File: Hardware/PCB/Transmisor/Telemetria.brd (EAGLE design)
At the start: 74.9 x 87.3 mm, 15 parts, among them X3 JST-XH-05-PIN-LONG-PAD

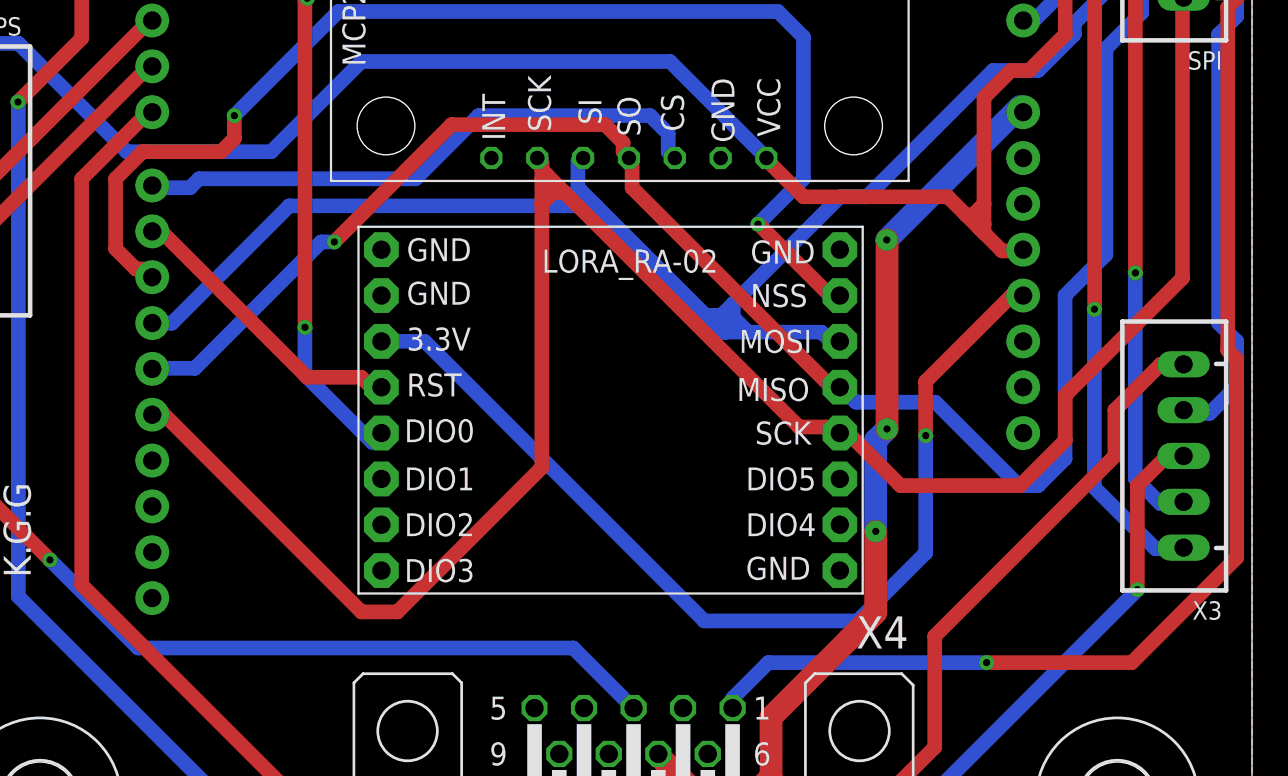
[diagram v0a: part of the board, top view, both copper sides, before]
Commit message: fix(transmissor): transmisson pcb updated
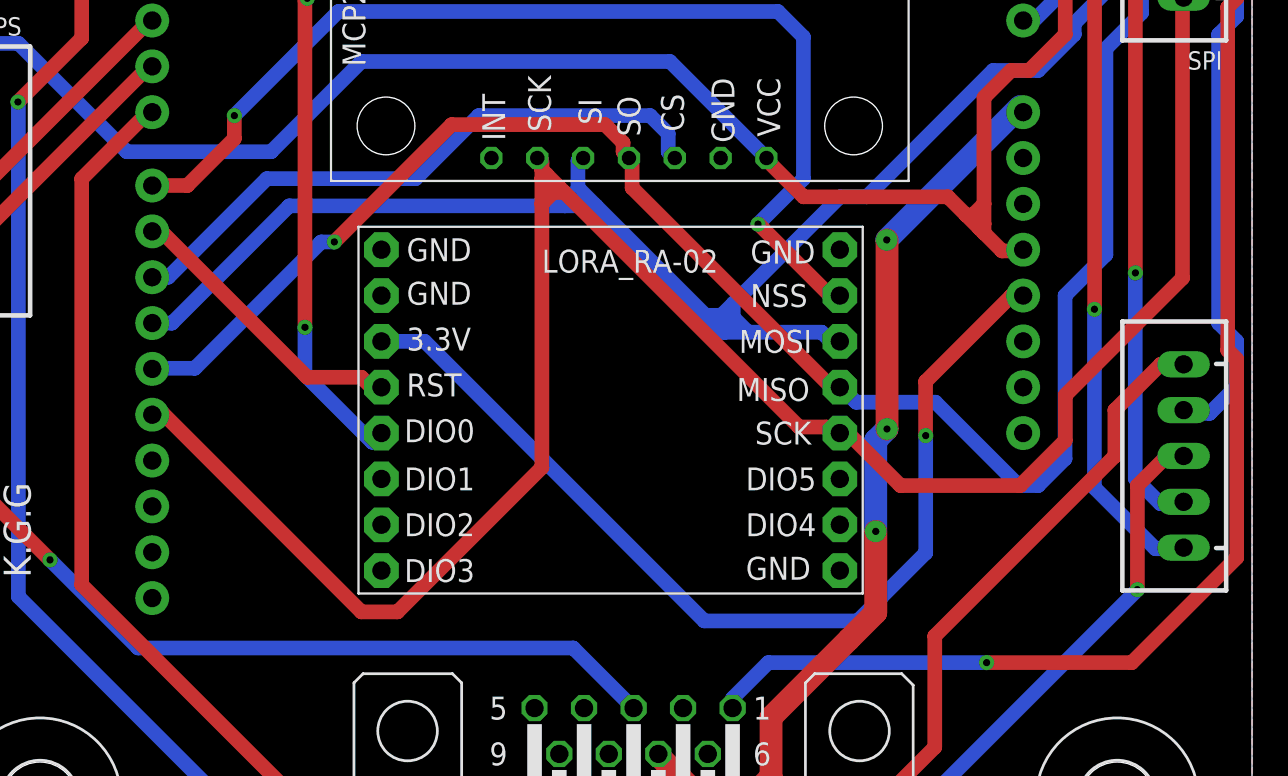
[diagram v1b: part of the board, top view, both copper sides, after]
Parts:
- LORA_STATUS_LED: value (none) -> BLUE
- MCP_STATUS_LED: value (none) -> RED
- R1: value (none) -> 150
- R10: value (none) -> 100
- X4: value (none) -> DV9
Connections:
- net LORA_NSS: now also B1.D8; no longer B1.D10
- net MCP_CS: now also B1.D10; no longer B1.D8
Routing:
- net LORA_NSS: track 67.5 -> 59.0 mm
- net MCP_CS: track 32.2 -> 34.2 mm
- net D7: track 111.5 -> 110.9 mm
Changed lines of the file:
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@@
 <attribute name="VALUE" x="2.54" y="-41.148" size="0.6096" layer="27" font="vector" ratio="20" align="top-center"/>
 </element>
-<element name="LORA_STATUS_LED" library="led" library_urn="urn:adsk.eagle:library:259" package="CHIP-LED0805" package3d_urn="urn:adsk.eagle:package:15818/1" value="" x="24.13" y="22.86" smashed="yes" rot="R270">
+<element name="LORA_STATUS_LED" library="led" library_urn="urn:adsk.eagle:library:259" package="CHIP-LED0805" package3d_urn="urn:adsk.eagle:package:15818/1" value="BLUE" x="24.13" y="22.86" smashed="yes" rot="R270">
 <attribute name="NAME" x="18.669" y="20.447" size="1.27" layer="25"/>
-<attribute name="VALUE" x="22.86" y="20.32" size="1.27" layer="27"/>
-</element>
-<element name="MCP_STATUS_LED" library="led" library_urn="urn:adsk.eagle:library:259" package="CHIP-LED0805" package3d_urn="urn:adsk.eagle:package:15818/1" value="" x="-17.78" y="21.59" smashed="yes" rot="R270">
+<attribute name="VALUE" x="34.163" y="24.13" size="1.27" layer="27"/>
+</element>
+<element name="MCP_STATUS_LED" library="led" library_urn="urn:adsk.eagle:library:259" package="CHIP-LED0805" package3d_urn="urn:adsk.eagle:package:15818/1" value="RED" x="-17.78" y="21.59" smashed="yes" rot="R270">
 <attribute name="NAME" x="-28.829" y="18.161" size="1.27" layer="25"/>
-<attribute name="VALUE" x="-19.05" y="19.05" size="1.27" layer="27"/>
-</element>
-<element name="R1" library="resistor" library_urn="urn:adsk.eagle:library:348" package="M0805" package3d_urn="urn:adsk.eagle:package:26079/1" value="" x="-25.4" y="21.59" smashed="yes">
+<attribute name="VALUE" x="-23.876" y="22.987" size="1.27" layer="27"/>
+</element>
+<element name="R1" library="resistor" library_urn="urn:adsk.eagle:library:348" package="M0805" package3d_urn="urn:adsk.eagle:package:26079/1" value="150" x="-25.4" y="21.59" smashed="yes">
 <attribute name="NAME" x="-26.67" y="22.86" size="1.27" layer="25"/>
-<attribute name="VALUE" x="-26.67" y="19.05" size="1.27" layer="27"/>
-</element>
-<element name="R10" library="resistor" library_urn="urn:adsk.eagle:library:348" package="M0805" package3d_urn="urn:adsk.eagle:package:26079/1" value="" x="31.75" y="22.86" smashed="yes">
+<attribute name="VALUE" x="-30.861" y="21.082" size="1.27" layer="27"/>
+</element>
+<element name="R10" library="resistor" library_urn="urn:adsk.eagle:library:348" package="M0805" package3d_urn="urn:adsk.eagle:package:26079/1" value="100" x="31.75" y="22.86" smashed="yes">
 <attribute name="NAME" x="30.48" y="24.13" size="1.27" layer="25"/>
-<attribute name="VALUE" x="30.48" y="20.32" size="1.27" layer="27"/>
+<attribute name="VALUE" x="34.29" y="22.352" size="1.27" layer="27"/>
 </element>
 <element name="GPS" library="Rembrandt Electronics - JST XH Connectors v1-0" package="JST-XH-05-PACKAGE-LONG-PAD" value="JST-XH-05-PIN-LONG-PAD" x="-31.75" y="-7.62" smashed="yes" rot="R270">
@@
 </element>
 <element name="X3" library="Rembrandt Electronics - JST XH Connectors v1-0" package="JST-XH-05-PACKAGE-LONG-PAD" value="JST-XH-05-PIN-LONG-PAD" x="35.56" y="-22.86" smashed="yes" rot="R90">
-<attribute name="NAME" x="37.7" y="-30.915" size="1.016" layer="25" ratio="10" rot="R180"/>
 <attribute name="VALUE" x="31.6675" y="-30.0625" size="0.8128" layer="27" ratio="10" rot="R90"/>
 </element>
-<element name="X4" library="con-subd" library_urn="urn:adsk.eagle:library:189" package="F09H" package3d_urn="urn:adsk.eagle:package:10276/1" value="" x="5.08" y="-38.1" smashed="yes" rot="R180">
+<element name="X4" library="con-subd" library_urn="urn:adsk.eagle:library:189" package="F09H" package3d_urn="urn:adsk.eagle:package:10276/1" value="DV9" x="5.08" y="-38.1" smashed="yes" rot="R180">
 <attribute name="MF" value="" x="5.08" y="-38.1" size="1.778" layer="27" rot="R180" display="off"/>
 <attribute name="MPN" value="" x="5.08" y="-38.1" size="1.778" layer="27" rot="R180" display="off"/>
-<attribute name="NAME" x="20.32" y="-31.75" size="1.778" layer="25" ratio="10" rot="R180"/>
 <attribute name="OC_FARNELL" value="unknown" x="5.08" y="-38.1" size="1.778" layer="27" rot="R180" display="off"/>
 <attribute name="OC_NEWARK" value="unknown" x="5.08" y="-38.1" size="1.778" layer="27" rot="R180" display="off"/>
 <attribute name="POPULARITY" value="0" x="5.08" y="-38.1" size="1.778" layer="27" rot="R180" display="off"/>
-<attribute name="VALUE" x="10.16" y="-52.07" size="1.778" layer="27" ratio="10" rot="R180"/>
 </element>
 <element name="MCP2515" library="EL_POTENCIA_LIBRERIA_VES2018" package="MCP2515" value="MCP2515" x="3.81" y="16.51" smashed="yes" rot="R270">
@@
 </signal>
 <signal name="MCP_CS">
-<contactref element="B1" pad="D8"/>
 <contactref element="MCP2515" pad="CS"/>
 <wire x1="7" y1="-5" x2="7" y2="-6" width="0.8128" layer="16"/>
 <wire x1="6" y1="-4" x2="7" y2="-5" width="0.8128" layer="16"/>
-<wire x1="-3.5" y1="-4" x2="6" y2="-4" width="0.8128" layer="16"/>
-<wire x1="-7" y1="-7.5" x2="-3.5" y2="-4" width="0.8128" layer="16"/>
-<wire x1="-19" y1="-7.5" x2="-7" y2="-7.5" width="0.8128" layer="16"/>
-<wire x1="-19.5" y1="-8" x2="-19" y2="-7.5" width="0.8128" layer="16"/>
-<wire x1="-21.5" y1="-8" x2="-19.5" y2="-8" width="0.8128" layer="16"/>
+<wire x1="6" y1="-4" x2="-3.5" y2="-4" width="0.8128" layer="16"/>
 <wire x1="7" y1="-6" x2="7.366" y2="-6.35" width="0.8128" layer="16"/>
-<wire x1="-21.5" y1="-8" x2="-21.59" y2="-7.874" width="0.8128" layer="16"/>
+<contactref element="B1" pad="D10"/>
+<wire x1="-15.24" y1="-7.493" x2="-20.701" y2="-12.954" width="0.8128" layer="16"/>
+<wire x1="-20.701" y1="-12.954" x2="-21.59" y2="-12.954" width="0.8128" layer="16"/>
+<wire x1="-3.5" y1="-4" x2="-6.993" y2="-7.493" width="0.8128" layer="16"/>
+<wire x1="-6.993" y1="-7.493" x2="-15.24" y2="-7.493" width="0.8128" layer="16"/>
 </signal>
 <signal name="GND">
@@
 <contactref element="B1" pad="D7"/>
 <contactref element="X3" pad="5"/>
-<wire x1="35.56" y1="-17.78" x2="35.014" y2="-17.78" width="0.8128" layer="1"/>
 <wire x1="21.77" y1="-39" x2="16.5" y2="-44.27" width="0.8128" layer="1"/>
 <wire x1="-11.23" y1="-44.27" x2="16.5" y2="-44.27" width="0.8128" layer="1"/>
@@
 <wire x1="-22" y1="-4" x2="-25.5" y2="-7.5" width="0.8128" layer="1"/>
 <wire x1="-22" y1="-4" x2="-21.59" y2="-3.81" width="0.8128" layer="1"/>
-<wire x1="35.56" y1="-17.78" x2="34.29" y2="-17.78" width="0.8128" layer="1"/>
 <wire x1="34.29" y1="-17.78" x2="31.75" y2="-20.32" width="0.8128" layer="1"/>
 <wire x1="31.75" y1="-20.32" x2="31.75" y2="-22.86" width="0.8128" layer="1"/>
 <wire x1="31.75" y1="-22.86" x2="21.77" y2="-32.84" width="0.8128" layer="1"/>
 <wire x1="21.77" y1="-32.84" x2="21.77" y2="-39" width="0.8128" layer="1"/>
+<wire x1="35.56" y1="-17.78" x2="34.29" y2="-17.78" width="0.8128" layer="1"/>
 </signal>
 <signal name="A0">
@@
 </signal>
 <signal name="LORA_NSS">
-<contactref element="B1" pad="D10"/>
 <contactref element="LORA_RA-02" pad="NSS"/>
-<wire x1="-22.5" y1="-12.5" x2="-22" y2="-12.5" width="0.8128" layer="1"/>
-<wire x1="-23.619" y1="-11.381" x2="-22.5" y2="-12.5" width="0.8128" layer="1"/>
-<wire x1="-23.619" y1="-7.5" x2="-23.619" y2="-11.381" width="0.8128" layer="1"/>
-<wire x1="-22.119" y1="-6" x2="-23.619" y2="-7.5" width="0.8128" layer="1"/>
-<wire x1="-17.77" y1="-6" x2="-22.119" y2="-6" width="0.8128" layer="1"/>
 <wire x1="-17.04" y1="-4" x2="-17.04" y2="-5.27" width="0.8128" layer="1"/>
-<wire x1="-17.04" y1="-5.27" x2="-17.77" y2="-6" width="0.8128" layer="1"/>
 <wire x1="-11.27" y1="1.77" x2="-17.04" y2="-4" width="0.8128" layer="16"/>
 <wire x1="13.08" y1="1.77" x2="-11.27" y2="1.77" width="0.8128" layer="16"/>
@@
 <wire x1="12.016" y1="-10.016" x2="11.976" y2="-10.016" width="0.8128" layer="1"/>
 <wire x1="16.5" y1="-14" x2="16" y2="-14" width="0.8128" layer="1"/>
-<wire x1="-22" y1="-12.5" x2="-21.59" y2="-12.954" width="0.8128" layer="1"/>
 <wire x1="16.5" y1="-14" x2="16.51" y2="-13.97" width="0.8128" layer="1"/>
 <via x="-17.04" y="-4" extent="1-16" drill="0.4"/>
 <via x="11.976" y="-10.016" extent="1-16" drill="0.4"/>
+<contactref element="B1" pad="D8"/>
+<wire x1="-19.644" y1="-7.874" x2="-21.59" y2="-7.874" width="0.8128" layer="1"/>
+<wire x1="-17.04" y1="-5.27" x2="-19.644" y2="-7.874" width="0.8128" layer="1"/>
 </signal>
 <signal name="VIN_12V">
